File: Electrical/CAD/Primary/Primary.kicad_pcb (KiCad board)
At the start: 2 copper layers, 2 parts

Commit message: End of Episode 7.
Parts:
- removed D1, D2: D_0603_1608Metric, Diode_SMD:D_0603_1608Metric
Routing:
- net (no net): track 106.1 -> 4594.4 mm

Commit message: Mid episode 10 commit.
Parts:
- added BT1: 2x_Battery_Cell, WirelessPower:Keystone_Dual_AA_Holder, F.Cu at (98.0, 56.4)
- added U2: MCP6282, Package_DIP:DIP-8_W7.62mm, F.Cu at (124.7, 82.4)
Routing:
- net (no net): track 4594.4 -> 3573.6 mm

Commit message: End of episode 10 commit.
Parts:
- added C1: 10nF, Capacitor_THT:CP_Radial_D6.3mm_P2.50mm, F.Cu at (142.6, 109.3)
- added C2: 10nF, Capacitor_THT:CP_Radial_D6.3mm_P2.50mm, F.Cu at (166.6, 115.3)
- added C3: 470pF, Capacitor_THT:CP_Radial_D6.3mm_P2.50mm, F.Cu at (186.6, 112.3)
- added C4: C, Capacitor_THT:CP_Radial_D6.3mm_P2.50mm, F.Cu at (177.6, 103.3)
- added L1: L, Jumper:SolderJumper-2_P1.3mm_Open_Pad1.0x1.5mm, F.Cu at (175.2, 89.3)
- added Q1: 2N3904, Package_TO_SOT_THT:TO-92_Inline, F.Cu at (207.6, 109.8)
- added Q2: 2N3906, Package_TO_SOT_THT:TO-92_Inline, F.Cu at (207.6, 118.6)
- added R1: 33k, Resistor_THT:R_Axial_DIN0207_L6.3mm_D2.5mm_P7.62mm_Horizontal, F.Cu at (161.6, 122.3)
- added R2: 1M, Resistor_THT:R_Axial_DIN0207_L6.3mm_D2.5mm_P7.62mm_Horizontal, F.Cu at (138.6, 117.3)
- added R3: 2.2k, Resistor_THT:R_Axial_DIN0207_L6.3mm_D2.5mm_P7.62mm_Horizontal, F.Cu at (180.6, 114.3)
- added R4: 5.1, Resistor_THT:R_Axial_DIN0207_L6.3mm_D2.5mm_P7.62mm_Horizontal, F.Cu at (201.6, 103.3)
- added SW1: SW_DPST, WirelessPower:GF-325, F.Cu at (142.6, 138.3)
- added U1: LMC555xN, Package_DIP:DIP-8_W7.62mm, F.Cu at (159.6, 117.3)
- moved BT1 119.2 mm to (182.0, 141.0)
- moved U2 75.9 mm to (193.6, 114.3)
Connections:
- BT1 pad 3: Net-(BT1-Pad3) -> GND
- U2 pad 1: Net-(U2-Pad1) -> Net-(C3-Pad1)
- U2 pad 3: Net-(U2-Pad3) -> +1V5
- U2 pad 4: Net-(U2-Pad4) -> GND
- U2 pad 5: Net-(U2-Pad5) -> Net-(C3-Pad1)
- U2 pad 8: Net-(U2-Pad8) -> +3V0
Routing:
- net +3V0: track 0.00 -> 127.9 mm
- net +1V5: track 0.00 -> 92.0 mm
- net Net-(BT1-Pad2): track 0.00 -> 77.8 mm
- net Net-(C2-Pad1): track 0.00 -> 31.8 mm
- net Net-(Q1-Pad1): track 0.00 -> 30.0 mm
- net Net-(R1-Pad1): track 0.00 -> 25.9 mm
- net Net-(BT1-Pad1): track 0.00 -> 18.8 mm
- net Net-(C3-Pad1): track 0.00 -> 18.6 mm
- net Net-(Q1-Pad2): track 0.00 -> 18.1 mm
- net Net-(C4-Pad1): track 0.00 -> 16.4 mm
- net Net-(C3-Pad2): track 0.00 -> 14.1 mm
- net Net-(C1-Pad1): track 0.00 -> 9.54 mm
- added copper zone on B.Cu, net GND

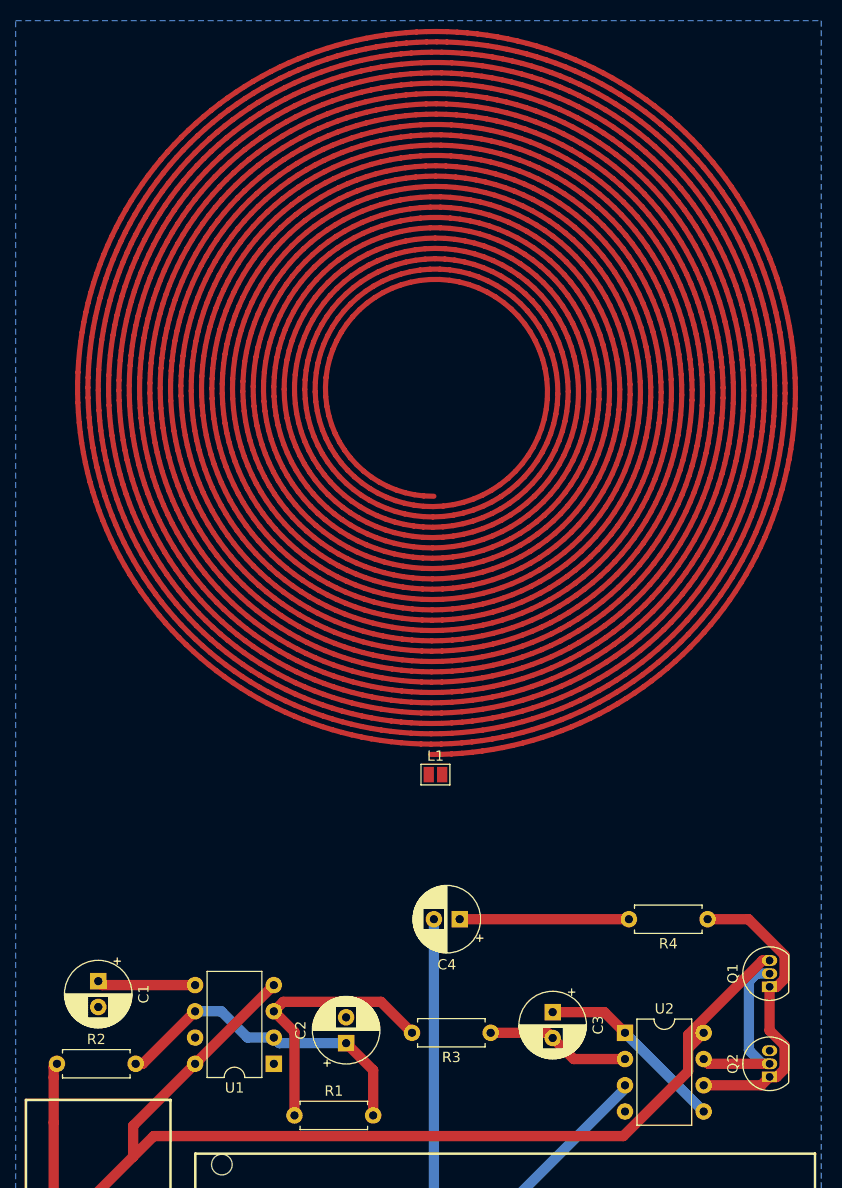
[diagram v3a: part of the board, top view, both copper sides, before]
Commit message: Update the PCB using the bezier curve spiral coil component. See primary-pcb-coil-bezier.png for a preview of the result.
It requires using the latest Nightly Development Builds from https://kicad-downloads.s3.cern.ch/index.html?prefix=windows/nightly/.
However, as noted in the previous commit, it will be very very slow to load (>15 minutes).
I have a patch for this issue that I will submit.
In the meantime, if anyone is interested to use this please contact me and I will send it to you.
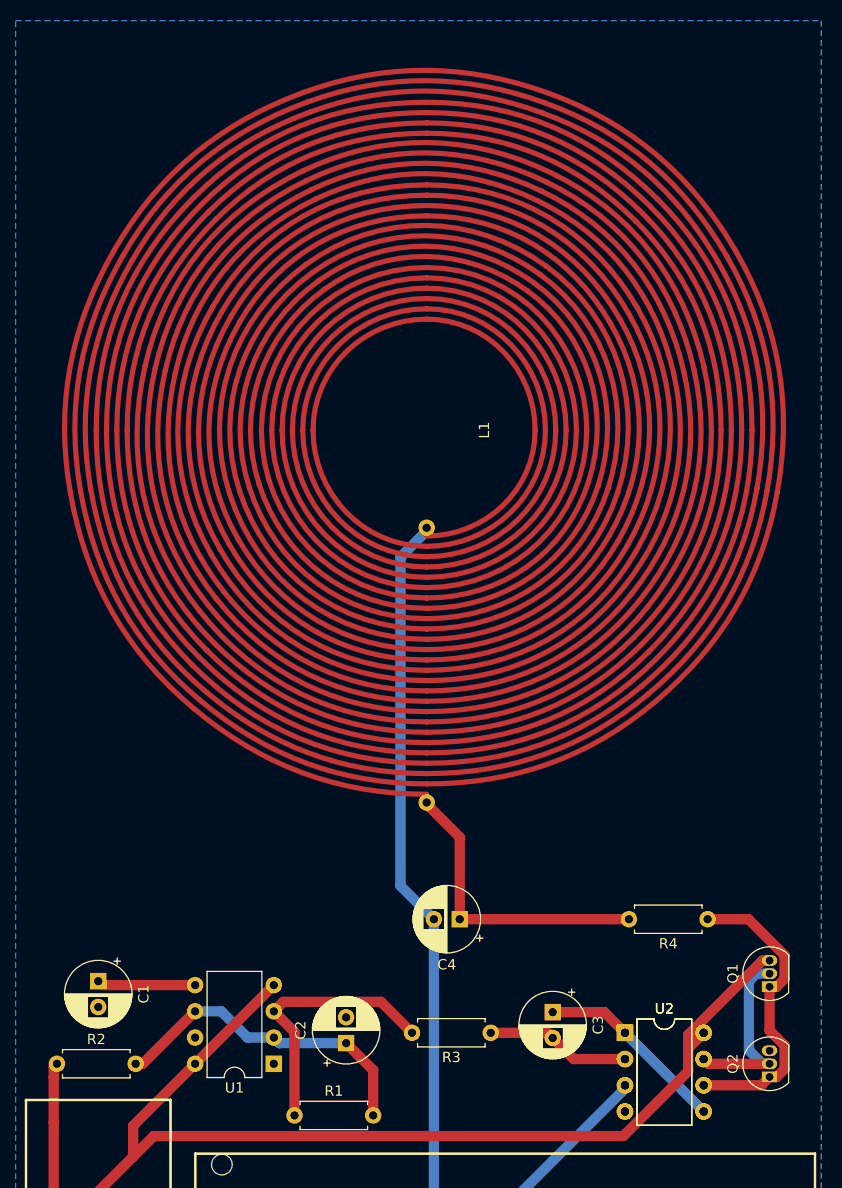
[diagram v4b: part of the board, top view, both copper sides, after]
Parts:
- added U2: MCP6282, Package_DIP:DIP-8_W7.62mm, F.Cu at (193.6, 114.3)
- L1: footprint Jumper:SolderJumper-2_P1.3mm_Open_Pad1.0x1.5mm -> WirelessPower:CoilSpiral_25_Bezier
- moved L1 33.4 mm to (174.4, 56.0), turned to 90 degrees
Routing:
- net (no net): track 3573.6 -> 0.00 mm
- net +1V5: track 92.0 -> 132.0 mm
- net Net-(C4-Pad1): track 16.4 -> 28.9 mm
